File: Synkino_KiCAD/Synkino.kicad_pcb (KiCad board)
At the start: 2 copper layers, 88.4 x 82.3 mm, 182 parts, among them J1 Conn_01x02_Male, J10 EYE8_OUT, J11 EYE4_OUT, J12 2.5mm, J13 EYE5_OUT, J2 2.5mm, J3 3.5mm, J4 Micro_SD_Card_Det_Hirose_DM3AT, J5 EYE1_OUT, J6 EYE6_OUT, J7 EYE2_OUT, J8 EYE7_OUT, J9 EYE3_OUT, Q1 IRF7319, Q2 BC847, SW1 SW_Push, SW2 Rotary_Encoder_Switch, SW3 SW_Push, U1 MCP1702T-5002E/MB, U10 ATMEGA328P-AU, U11 QRE1113, U12 QRE1113, U13 QRE1113, U14 QRE1113, U15 QRE1113, U16 QRE1113, U18 QRE1113, U2 ATMEGA328P-AU, U3 74HC4050, U4 SPIOLED128x64, U5 AP7312-1833W6-7, U6 74HC14, U7 VS1053B, U8 MAX4741, U9 QRE1113, X1 FTDIconn, X2 ICSP, X3 FTDIconn, X4 ICSP, Y1 16Mhz, Y2 12.288MHz, Y3 16Mhz

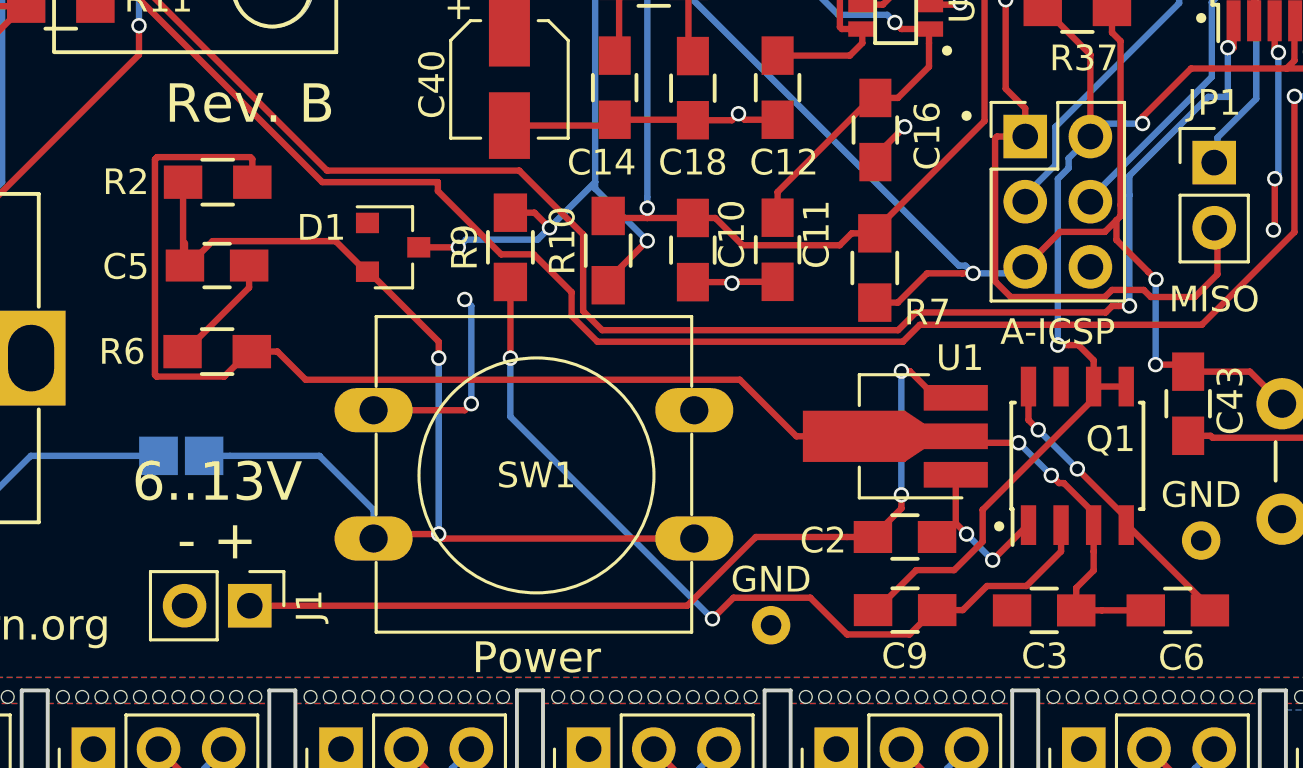
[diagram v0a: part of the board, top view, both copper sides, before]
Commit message: Fixing PCB for LDO Pinout Bug
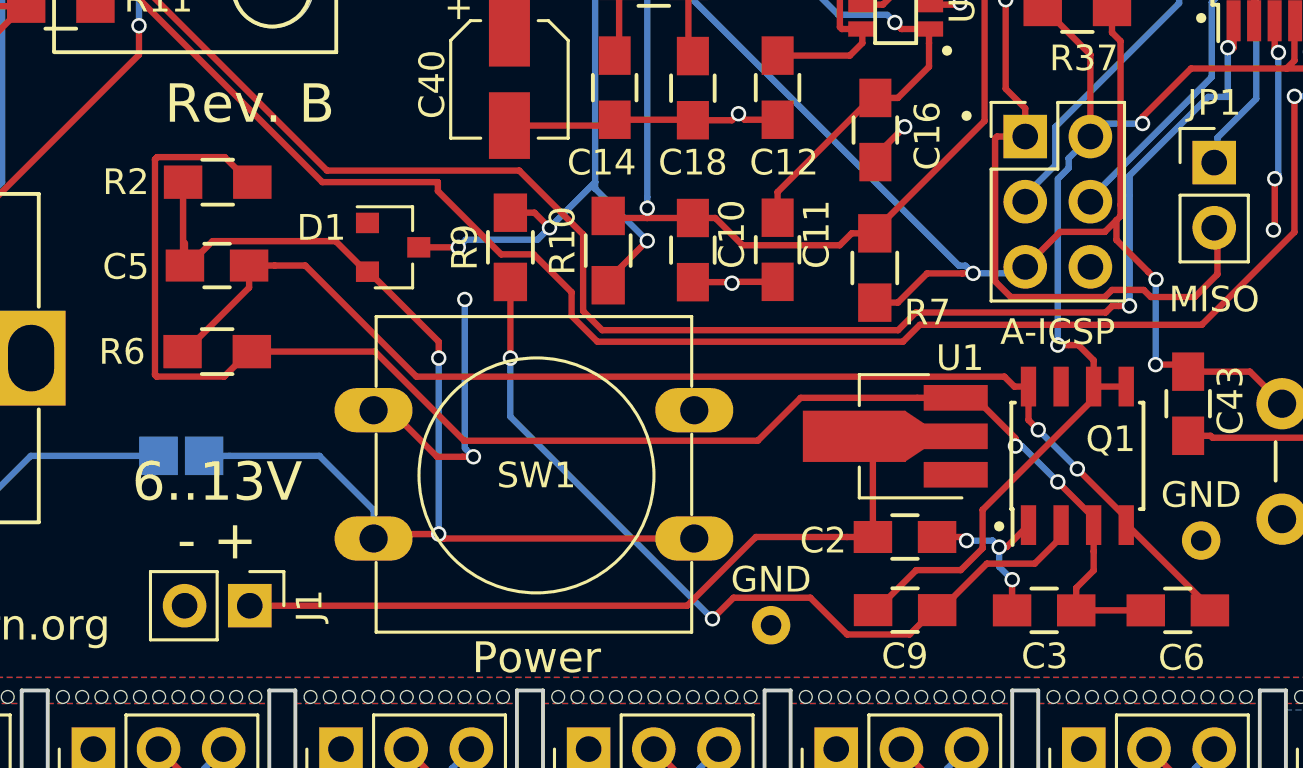
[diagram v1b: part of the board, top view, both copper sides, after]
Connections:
- C6 pad 1: Net-(C6-Pad1) -> Net-(C5-Pad1)
- Q1 pad 4: Net-(C6-Pad1) -> Net-(C5-Pad1)
- Q1 pad 8: Net-(C6-Pad1) -> Net-(C5-Pad1)
- SW2 pad 1: Net-(P.On2-Pad1) -> Net-(SW2-Pad1)
- U1 pad 2: Net-(C3-Pad2) -> Net-(C2-Pad1)
- U1 pad 3: Net-(C2-Pad1) -> Net-(C3-Pad2)
- U2 pad 2: Net-(P.On2-Pad1) -> Net-(SW2-Pad1)
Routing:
- net Net-(SW2-Pad1): track 0.00 -> 45.7 mm, vias 0 -> 1
- net Net-(P.On2-Pad1): track 50.6 -> 4.98 mm, vias 1 -> 0
- net Net-(C5-Pad1): track 4.59 -> 48.5 mm, vias 0 -> 2
- net Net-(C6-Pad1): track 11.6 -> 0.00 mm, vias 2 -> 0
- net GND: track 203.8 -> 207.5 mm, vias 49 -> 50
- net Net-(C3-Pad2): track 61.4 -> 60.5 mm
- net Net-(C2-Pad1): track 35.0 -> 35.3 mm, vias 2 -> 0

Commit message: Minor Schematic Tweaks
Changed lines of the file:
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@@
 (kicad_pcb (version 4) (host pcbnew 4.0.7)
   (general
-    (links 388)
-    (no_connects 19)
-    (area 71.552999 38.024999 160.095001 120.471001)
+    (links 372)
+    (no_connects 0)
+    (area 62.682429 32.843999 168.838572 132.270286)
     (thickness 1.6)
     (drawings 90)
-    (tracks 2051)
+    (tracks 2050)
     (zones 0)
     (modules 182)
@@
   (segment (start 100.584 56.134) (end 100.584 56.896) (width 0.25) (layer B.Cu) (net 6))
   (segment (start 100.584 56.896) (end 100.584 56.642) (width 0.25) (layer B.Cu) (net 6))
-  (segment (start 106.934 50.272) (end 106.446 50.272) (width 0.25) (layer F.Cu) (net 6))
   (segment (start 75.184 97.79) (end 85.461002 97.79) (width 0.25) (layer F.Cu) (net 6))
   (segment (start 100.584 82.667002) (end 100.584 81.534) (width 0.25) (layer F.Cu) (net 6))

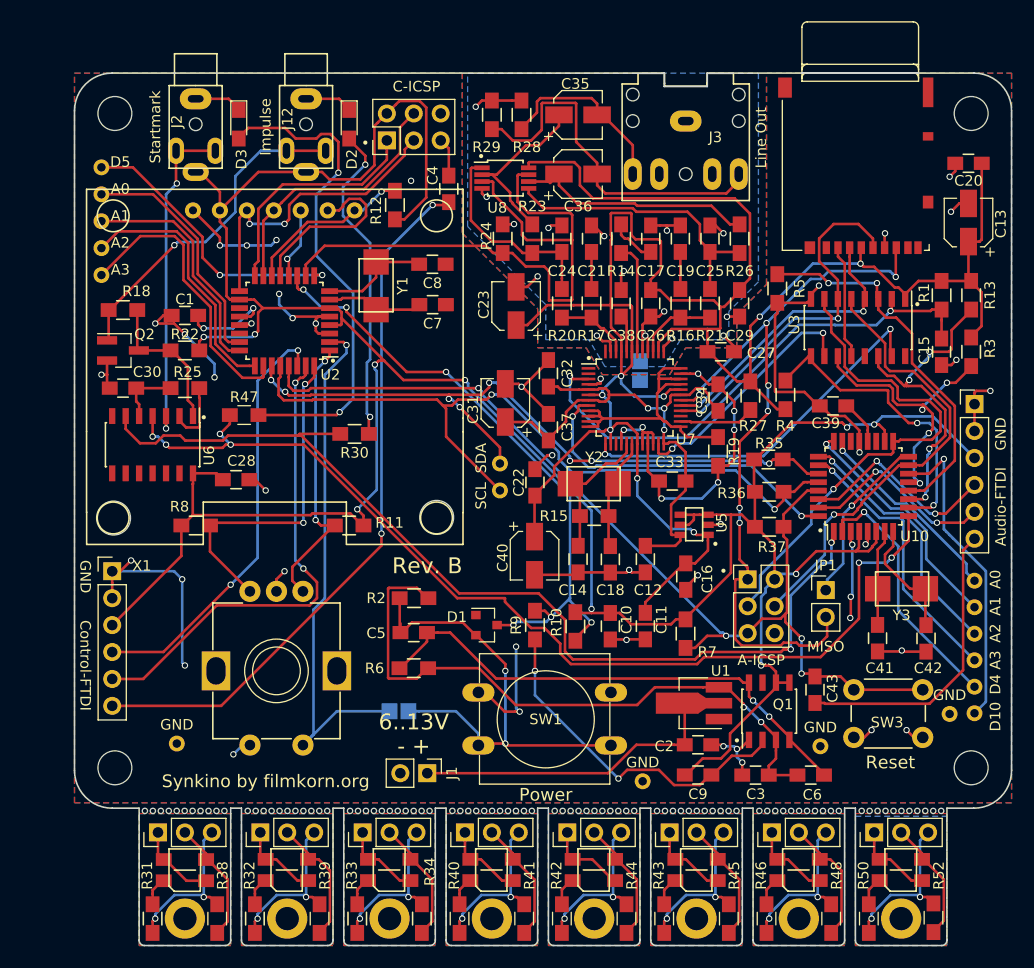
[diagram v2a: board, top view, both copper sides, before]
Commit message: Reverse Polarity Protection Tweaks
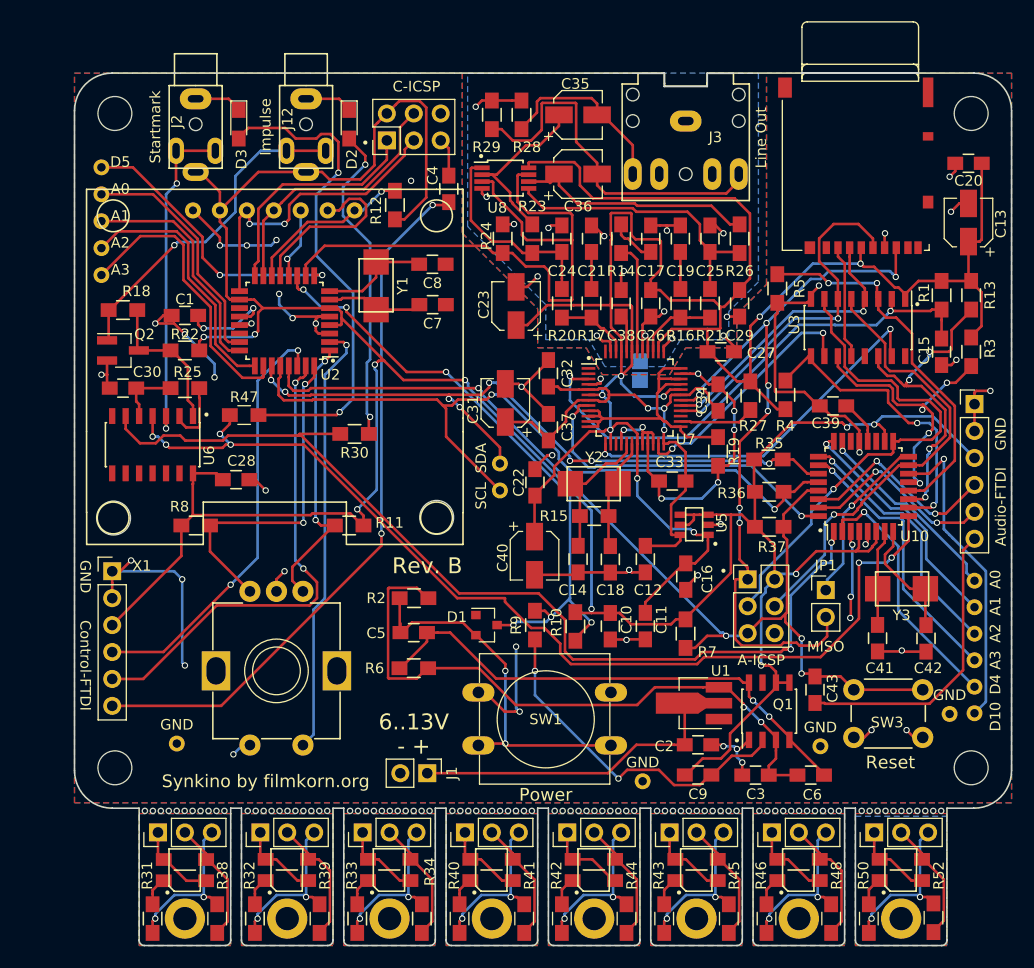
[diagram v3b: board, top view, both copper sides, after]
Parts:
- removed P.On1, P.On2: P.On, Measurement_Points:Measurement_Point_Square-SMD-Pad_Small
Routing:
- net Net-(C5-Pad2): track 44.8 -> 36.2 mm
- net Net-(P.On2-Pad1): track 4.98 -> 0.00 mm
- net Net-(SW2-Pad1): track 45.7 -> 41.1 mm
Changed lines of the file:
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@@
     (area 62.682429 32.843999 168.838572 132.270286)
     (thickness 1.6)
-    (drawings 90)
-    (tracks 2050)
+    (drawings 98)
+    (tracks 2044)
     (zones 0)
-    (modules 182)
-    (nets 135)
+    (modules 180)
+    (nets 134)
   )
   (page A4)
@@
   (net 131 "Net-(D3-Pad2)")
   (net 132 "Net-(J12-Pad2)")
-  (net 133 "Net-(P.On2-Pad1)")
-  (net 134 "Net-(SW2-Pad1)")
+  (net 133 "Net-(SW2-Pad1)")
   (net_class Default "This is the default net class."
     (clearance 0.2)
@@
     (fp_circle (center 5 -5.5) (end 5.5 -5.5) (layer Dwgs.User) (width 0.1))
     (pad 1 thru_hole circle (at -2.5 -7 180) (size 2 2) (drill 1) (layers *.Cu *.Mask)
-      (net 134 "Net-(SW2-Pad1)"))
+      (net 133 "Net-(SW2-Pad1)"))
     (pad A thru_hole circle (at -2.5 7.5 180) (size 2 2) (drill 1) (layers *.Cu *.Mask)
       (net 51 "Net-(R11-Pad1)"))
@@
       (net 51 "Net-(R11-Pad1)"))
     (pad 2 smd rect (at -4.25 -2 180) (size 1.6 0.55) (layers F.Cu F.Paste F.Mask)
-      (net 134 "Net-(SW2-Pad1)"))
+      (net 133 "Net-(SW2-Pad1)"))
     (pad 3 smd rect (at -4.25 -1.2 180) (size 1.6 0.55) (layers F.Cu F.Paste F.Mask)
       (net 2 GND))
@@
     )
   )
-  (module Measurement_Points:Measurement_Point_Square-SMD-Pad_Small (layer B.Cu)
-    (at 103.124 98.298)
-    (descr "Mesurement Point, Square, SMD Pad,  1.5mm x 1.5mm,")
-    (tags "Mesurement Point Square SMD Pad 1.5x1.5mm")
-    (attr virtual)
-    (fp_text reference P.On1 (at 0 2) (layer B.SilkS) hide
-      (effects (font (size 1 1) (thickness 0.15)) (justify mirror))
-    )
-    (fp_text value P.On (at 0 -2) (layer B.Fab) hide
-      (effects (font (size 1 1) (thickness 0.15)) (justify mirror))
-    )
-    (fp_line (start -1 1) (end 1 1) (layer B.CrtYd) (width 0.05))
-    (fp_line (start 1 1) (end 1 -1) (layer B.CrtYd) (width 0.05))
-    (fp_line (start 1 -1) (end -1 -1) (layer B.CrtYd) (width 0.05))
-    (fp_line (start -1 -1) (end -1 1) (layer B.CrtYd) (width 0.05))
-    (pad 1 smd rect (at 0 0) (size 1.5 1.5) (layers B.Cu B.Mask)
-      (net 8 "Net-(C5-Pad2)"))
-  )
-  (module Measurement_Points:Measurement_Point_Square-SMD-Pad_Small (layer B.Cu)
-    (at 101.346 98.298)
-    (descr "Mesurement Point, Square, SMD Pad,  1.5mm x 1.5mm,")
-    (tags "Mesurement Point Square SMD Pad 1.5x1.5mm")
-    (attr virtual)
-    (fp_text reference P.On2 (at 0 2) (layer B.SilkS) hide
-      (effects (font (size 1 1) (thickness 0.15)) (justify mirror))
-    )
-    (fp_text value P.On (at 0 -2) (layer B.Fab) hide
-      (effects (font (size 1 1) (thickness 0.15)) (justify mirror))
-    )
-    (fp_line (start -1 1) (end 1 1) (layer B.CrtYd) (width 0.05))
-    (fp_line (start 1 1) (end 1 -1) (layer B.CrtYd) (width 0.05))
-    (fp_line (start 1 -1) (end -1 -1) (layer B.CrtYd) (width 0.05))
-    (fp_line (start -1 -1) (end -1 1) (layer B.CrtYd) (width 0.05))
-    (pad 1 smd rect (at 0 0) (size 1.5 1.5) (layers B.Cu B.Mask)
-      (net 133 "Net-(P.On2-Pad1)"))
-  )
   (module Housings_SSOP:MSOP-8_3x3mm_Pitch0.65mm (layer F.Cu)
     (at 112.268 48.006)
@@
     )
   )
+  (gr_text • (at 80.391 115.443) (layer F.SilkS)
+    (effects (font (size 1 1) (thickness 0.2)))
+  )
+  (gr_text • (at 90.043 115.443) (layer F.SilkS)
+    (effects (font (size 1 1) (thickness 0.2)))
+  )
+  (gr_text • (at 99.695 115.443) (layer F.SilkS)
+    (effects (font (size 1 1) (thickness 0.2)))
+  )
+  (gr_text • (at 109.347 115.443) (layer F.SilkS)
+    (effects (font (size 1 1) (thickness 0.2)))
+  )
+  (gr_text • (at 118.999 115.443) (layer F.SilkS)
+    (effects (font (size 1 1) (thickness 0.2)))
+  )
+  (gr_text • (at 128.651 115.443) (layer F.SilkS)
+    (effects (font (size 1 1) (thickness 0.2)))
+  )
+  (gr_text • (at 138.303 115.443) (layer F.SilkS)
+    (effects (font (size 1 1) (thickness 0.2)))
+  )
+  (gr_text • (at 147.955 115.443) (layer F.SilkS)
+    (effects (font (size 1 1) (thickness 0.2)))
+  )
   (gr_text • (at 134.112 101.092) (layer F.SilkS)
     (effects (font (size 1 1) (thickness 0.2)))
@@
     (effects (font (size 1 1) (thickness 0.2)))
   )
-  (gr_text • (at 83.82 70.612) (layer F.SilkS)
+  (gr_text • (at 84.074 70.358) (layer F.SilkS)
     (effects (font (size 1 1) (thickness 0.2)))
   )
@@
   (segment (start 142.326 104.217) (end 142.326 104.321) (width 0.25) (layer F.Cu) (net 7))
   (segment (start 139.107 100.998) (end 142.326 104.217) (width 0.25) (layer F.Cu) (net 7))
-  (segment (start 109.728 101.52) (end 109.728 100.4064) (width 0.25) (layer B.Cu) (net 8))
-  (segment (start 109.728 100.4064) (end 107.6196 98.298) (width 0.25) (layer B.Cu) (net 8))
-  (segment (start 107.6196 98.298) (end 104.124 98.298) (width 0.25) (layer B.Cu) (net 8))
-  (segment (start 104.124 98.298) (end 103.124 98.298) (width 0.25) (layer B.Cu) (net 8))
   (segment (start 122.228 101.52) (end 112.442 101.52) (width 0.25) (layer F.Cu) (net 8))
   (segment (start 112.442 101.52) (end 112.268 101.346) (width 0.25) (layer F.Cu) (net 8))
@@
   (segment (start 81.046847 54.355153) (end 81.046847 54.335153) (width 0.25) (layer F.Cu) (net 132))
   (segment (start 91.622 45.426) (end 95.322 45.426) (width 0.25) (layer F.Cu) (net 132))
-  (segment (start 96.368 98.298) (end 101.346 98.298) (width 0.25) (layer B.Cu) (net 133))
-  (segment (start 93.178 101.488) (end 96.368 98.298) (width 0.25) (layer B.Cu) (net 134))
-  (segment (start 95.25 66.548) (end 97.282 64.516) (width 0.25) (layer B.Cu) (net 134))
-  (segment (start 97.282 64.516) (end 97.282 63.754) (width 0.25) (layer B.Cu) (net 134))
-  (segment (start 94.177999 88.702001) (end 95.25 87.63) (width 0.25) (layer B.Cu) (net 134))
-  (segment (start 95.25 87.63) (end 95.25 66.548) (width 0.25) (layer B.Cu) (net 134))
-  (segment (start 93.178 101.488) (end 94.177999 100.488001) (width 0.25) (layer B.Cu) (net 134))
-  (segment (start 94.177999 100.488001) (end 94.177999 88.702001) (width 0.25) (layer B.Cu) (net 134))
-  (segment (start 97.282 63.754) (end 96.996 63.468) (width 0.25) (layer F.Cu) (net 134))
-  (segment (start 96.996 63.468) (end 95.69 63.468) (width 0.25) (layer F.Cu) (net 134))
-  (via (at 97.282 63.754) (size 0.6) (drill 0.4) (layers F.Cu B.Cu) (net 134))
+  (segment (start 95.25 66.548) (end 97.282 64.516) (width 0.25) (layer B.Cu) (net 133))
+  (segment (start 97.282 64.516) (end 97.282 63.754) (width 0.25) (layer B.Cu) (net 133))
+  (segment (start 94.177999 88.702001) (end 95.25 87.63) (width 0.25) (layer B.Cu) (net 133))
+  (segment (start 95.25 87.63) (end 95.25 66.548) (width 0.25) (layer B.Cu) (net 133))
+  (segment (start 93.178 101.488) (end 94.177999 100.488001) (width 0.25) (layer B.Cu) (net 133))
+  (segment (start 94.177999 100.488001) (end 94.177999 88.702001) (width 0.25) (layer B.Cu) (net 133))
+  (segment (start 97.282 63.754) (end 96.996 63.468) (width 0.25) (layer F.Cu) (net 133))
+  (segment (start 96.996 63.468) (end 95.69 63.468) (width 0.25) (layer F.Cu) (net 133))
+  (via (at 97.282 63.754) (size 0.6) (drill 0.4) (layers F.Cu B.Cu) (net 133))
   (zone (net 88) (net_name GNDA) (layer B.Cu) (hatch edge 0.508)
     (connect_pads (clearance 0.508))

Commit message: Almost routed, D4 glitch still acts up
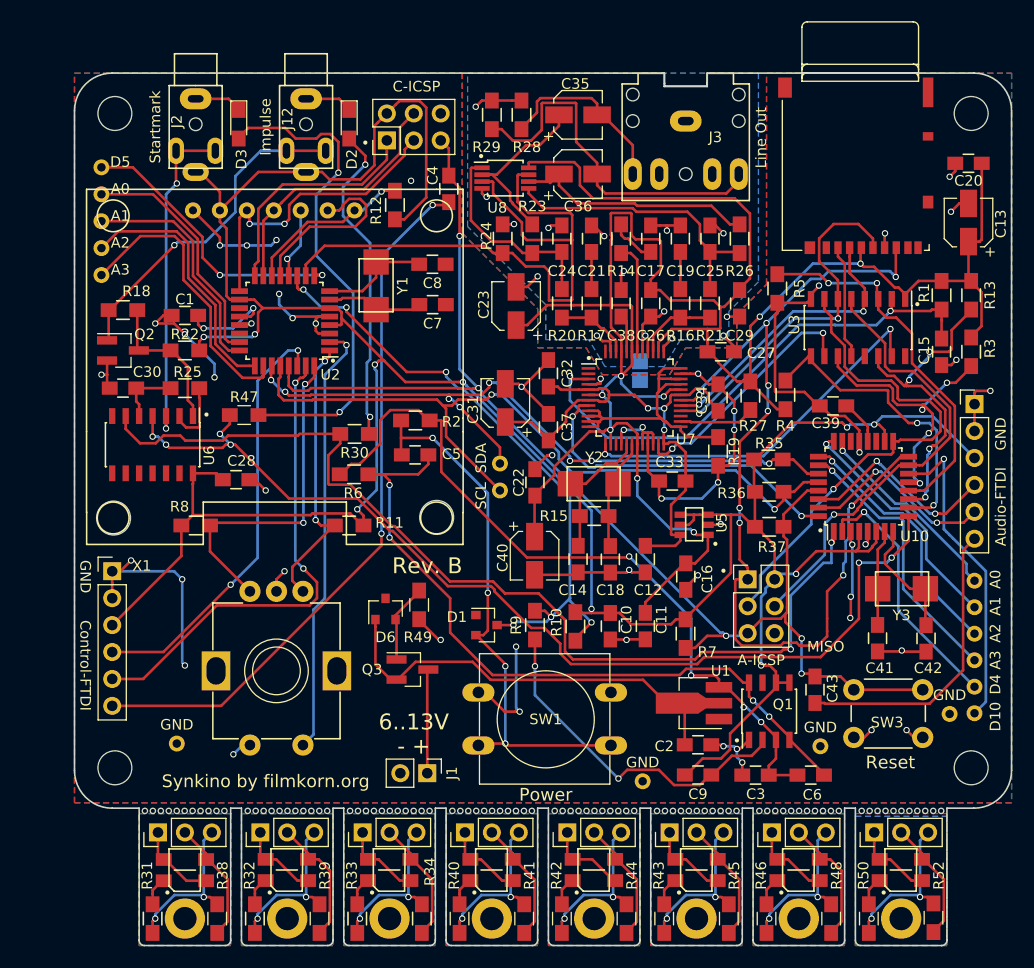
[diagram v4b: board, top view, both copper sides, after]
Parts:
- removed JP1: , Pin_Headers:Pin_Header_Straight_1x02_Pitch2.54mm
- added D6: BZX84C9V1, lib_fp:D_SOT-23_1A3K, F.Cu at (101.0, 88.6)
- added Q3: IRLML2244, TO_SOT_Packages_SMD:SOT-23_Handsoldering, F.Cu at (103.5, 94.4)
- added R49: 100k, Resistors_SMD:R_0805_HandSoldering, F.Cu at (104.1, 88.3)
- D4: value AD4 -> BZX84C9V1
- J1: value Conn_01x02_Male -> Pwr
- R30: value 270 -> 470
- moved R6 19.1 mm to (98.0, 75.9), turned to 0 degrees
- moved C5 16.8 mm to (103.8, 74.1)
- moved R2 16.8 mm to (103.8, 70.9)
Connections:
- C4 pad 1: /CTRL_RST -> /~RST
- D4 pad 1: Net-(AD4-Pad1) -> Net-(C2-Pad1)
- J1 pad 1: Net-(C2-Pad1) -> Net-(J1-Pad1)
- U10 pad 16: Net-(JP1-Pad1) -> /MISO_3V
- X2 pad 5: /CTRL_RST -> /~RST
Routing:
- net Net-(C2-Pad1): track 35.3 -> 68.6 mm, vias 0 -> 1
- net /~RST: track 96.3 -> 121.2 mm, vias 4 -> 5
- net Net-(AD4-Pad1): track 24.2 -> 1.05 mm, vias 1 -> 0
- net /MISO_3V: track 72.2 -> 91.1 mm, vias 7 -> 9
- net Net-(C5-Pad1): track 48.5 -> 67.1 mm, vias 2 -> 4
- net Net-(JP1-Pad1): track 16.3 -> 0.00 mm, vias 1 -> 0
- net Net-(C5-Pad2): track 36.2 -> 52.0 mm, vias 2 -> 4
- net Net-(C3-Pad2): track 60.5 -> 71.0 mm, vias 2 -> 4
- net Net-(J1-Pad1): track 0.00 -> 9.82 mm
- net Net-(D6-Pad2): track 0.00 -> 7.45 mm
- net /CTRL_RST: track 3.64 -> 0.00 mm
- net GND: track 207.5 -> 210.4 mm, vias 50 -> 51

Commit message: Versuchen, den HEAD zu retten
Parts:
- removed D6: BZX84C9V1, lib_fp:D_SOT-23_1A3K
- removed the GND at (125.2, 104.9)
- added D7: BZX84C9V1, lib_fp:D_SOT-23_1A3K, F.Cu at (101.6, 87.5)
- D4: value BZX84C9V1 -> AD4
- Q3: footprint TO_SOT_Packages_SMD:SOT-23_Handsoldering -> TO_SOT_Packages_SMD:SOT-23
- R30: value 470 -> 330
- moved R10 15.2 mm to (124.8, 104.3), turned to 180 degrees
- moved R9 14.6 mm to (125.1, 100.7)
- moved D3 12.2 mm to (74.9, 42.9)
- moved R49 6.83 mm to (106.3, 94.7)
- moved GND 6.35 mm to (74.9, 101.5)
- moved D1 5.51 mm to (105.7, 87.5), turned to 90 degrees
- moved C10 5.21 mm to (125.6, 86.4)
- moved   4.95 mm to (70.5, 103.6)
- moved   4.95 mm to (70.5, 41.9)
- moved X1 4.83 mm to (70.4, 85.1)
- moved SW1 4.49 mm to (109.7, 92.0)
- moved A0 3.81 mm to (70.4, 49.5)
- moved A1 3.81 mm to (70.4, 52.1)
- moved A2 3.81 mm to (70.4, 54.6)
- moved A3 3.81 mm to (70.4, 57.1)
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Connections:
- D4 pad 1: Net-(C2-Pad1) -> Net-(AD4-Pad1)
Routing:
- net Net-(AD4-Pad1): track 1.05 -> 24.2 mm, vias 0 -> 1
- net GND: track 210.4 -> 189.1 mm, vias 51 -> 46
- net Net-(C2-Pad1): track 68.6 -> 47.6 mm, vias 1 -> 0
- net Net-(C9-Pad2): track 33.0 -> 16.6 mm, vias 2 -> 0
- net /MISO_3V: track 91.1 -> 78.7 mm, vias 9 -> 8
- net Net-(D3-Pad2): track 46.9 -> 58.9 mm
- net /~PWR_OFF: track 60.4 -> 70.7 mm, vias 6 -> 5
- net Net-(C3-Pad2): track 71.0 -> 76.8 mm, vias 4 -> 6
- net +3V3: track 219.3 -> 224.8 mm
- net Net-(C4-Pad2): track 67.7 -> 72.6 mm
- net /CTRL_TXD: track 45.8 -> 50.6 mm
- net /CTRL_RXD: track 40.6 -> 45.4 mm
- net Net-(CD5-Pad1): track 27.0 -> 30.8 mm
- net Net-(CA3-Pad1): track 27.5 -> 31.3 mm
- net Net-(CA2-Pad1): track 24.5 -> 28.3 mm
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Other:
- board size 88.4 x 82.3 mm -> 93.3 x 82.3 mm
- board text added: "FTDI-A"
- board text added: "FTDI-C"
- board text added: "SCL"
- board text added: "SDA"
- board text added: "Synkino • Rev. B"
- board text removed: "MISO"
- board text removed: "Rev. B"
